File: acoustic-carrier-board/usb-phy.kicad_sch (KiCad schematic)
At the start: 53 parts, among them J801 TYPE-C-31-M-12, U801 USB3300-EZK, U802 LMV321, Y801 Crystal_GND24_Small

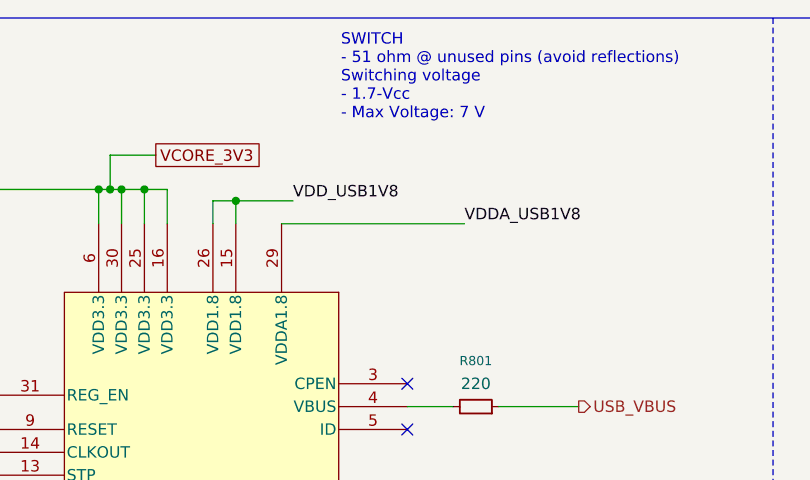
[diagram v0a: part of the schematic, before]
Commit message: Modified readme, removed testpoints and stubs, changed simulation folder structure, removed excess length matching
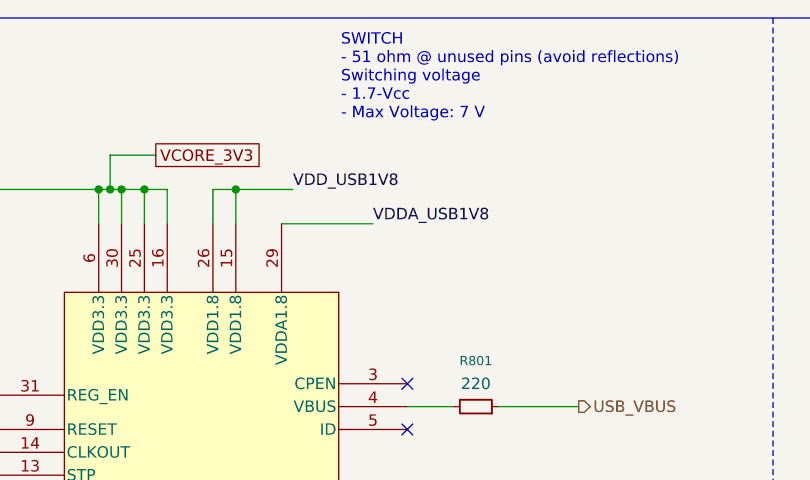
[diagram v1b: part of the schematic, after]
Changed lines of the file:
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@@
+	)
+	(junction
+		(at 160.02 38.1)
+		(diameter 0)
+		(color 0 0 0 0)
 	)
 	(junction
@@
 	(junction
 		(at 185.42 105.41)
-		(diameter 0)
-		(color 0 0 0 0)
-	)
-	(junction
-		(at 160.02 39.37)
 		(diameter 0)
 		(color 0 0 0 0)
@@
 	(wire
 		(pts
-			(xy 157.48 39.37) (xy 157.48 41.91)
+			(xy 157.48 38.1) (xy 157.48 41.91)
 		)
 		(stroke
@@
 	(wire
 		(pts
-			(xy 165.1 41.91) (xy 185.42 41.91)
+			(xy 165.1 41.91) (xy 175.26 41.91)
 		)
 		(stroke
@@
 	(wire
 		(pts
-			(xy 160.02 39.37) (xy 160.02 41.91)
+			(xy 160.02 38.1) (xy 160.02 41.91)
 		)
 		(stroke
@@
 	(wire
 		(pts
-			(xy 160.02 39.37) (xy 166.37 39.37)
+			(xy 160.02 38.1) (xy 166.37 38.1)
 		)
 		(stroke
@@
 	(wire
 		(pts
-			(xy 160.02 39.37) (xy 157.48 39.37)
+			(xy 160.02 38.1) (xy 157.48 38.1)
 		)
 		(stroke
@@
 	)
 	(label "VDD_USB1V8"
-		(at 166.37 39.37 0)
+		(at 166.37 38.1 0)
 		(effects
 			(font
@@
 	)
 	(label "VDDA_USB1V8"
-		(at 185.42 41.91 0)
+		(at 175.26 41.91 0)
 		(effects
 			(font

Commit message: added step-files
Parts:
- C801, C807, C808, C809, C810, C811, C812, C816, C820, C821, C822: LCSC Part Number (none) -> C22435929; LPN C22435929 -> (none); MPN CGA0201X7R104K160ET -> (none); Manufacturing Part Number (none) -> CGA0201X7R104K160ET
- C802, C817, C825: LCSC Part Number (none) -> C285010; LPN C285010 -> (none); MPN 0201B103K250NT -> (none); Manufacturing Part Number (none) -> 0201B103K250NT
- C803, C806: LCSC Part Number (none) -> C1555; LPN C1555 -> (none); MPN 0402CG220J500NT -> (none); Manufacturing Part Number (none) -> 0402CG220J500NT
- C804, C805: LCSC Part Number (none) -> C1530; LPN C1530 -> (none); MPN 0402B221K500NT -> (none); Manufacturing Part Number (none) -> 0402B221K500NT
- C813, C814, C819: LCSC Part Number (none) -> C23733; LPN C23733 -> (none); MPN CL05A475MP5NRNC -> (none); Manufacturing Part Number (none) -> CL05A475MP5NRNC
- C815: LCSC Part Number (none) -> C9196; LPN C9196 -> (none); MPN 1206B102K202NT -> (none); Manufacturing Part Number (none) -> 1206B102K202NT
- D801, D802: LCSC Part Number (none) -> C2286; LPN C2286 -> (none); MPN KT-0603R -> (none); Manufacturing Part Number (none) -> KT-0603R
- J801: LCSC Part Number (none) -> C165948; LPN C165948 -> (none); MPN TYPE-C-31-M-12 -> (none); Manufacturing Part Number (none) -> TYPE-C-31-M-12
- L801: LCSC Part Number (none) -> C113030; LPN C113030 -> (none); MPN BLM18SG121TN1D -> (none); Manufacturing Part Number (none) -> BLM18SG121TN1D
- R801: LCSC Part Number (none) -> C22962; LPN C22962 -> (none); MPN 0603WAF2200T5E -> (none); Manufacturing Part Number (none) -> 0603WAF2200T5E
- R802, R812: LCSC Part Number (none) -> C23018; LPN C23018 -> (none); MPN 0603WAF3901T5E -> (none); Manufacturing Part Number (none) -> 0603WAF3901T5E
- R803, R811: LCSC Part Number (none) -> C25803; LPN C25803 -> (none); MPN 0603WAF1003T5E -> (none); Manufacturing Part Number (none) -> 0603WAF1003T5E
- R804, R805: LCSC Part Number (none) -> C23186; LPN C23186 -> (none); MPN 0603WAF5101T5E -> (none); Manufacturing Part Number (none) -> 0603WAF5101T5E
- R806: LCSC Part Number (none) -> C26083; LPN C26083 -> (none); MPN 0402WGF1004TCE -> (none); Manufacturing Part Number (none) -> 0402WGF1004TCE
- R807: LCSC Part Number (none) -> C17168; LPN C17168 -> (none); MPN 0402WGF0000TCE -> (none); Manufacturing Part Number (none) -> 0402WGF0000TCE
- R808: LCSC Part Number (none) -> C22790; LPN C22790 -> (none); MPN 0603WAF1202T5E -> (none); Manufacturing Part Number (none) -> 0603WAF1202T5E
- R809, R810: LCSC Part Number (none) -> C4216; LPN C4216 -> (none); MPN 0603WAF3302T5E -> (none); Manufacturing Part Number (none) -> 0603WAF3302T5E
- R813, R821: LCSC Part Number (none) -> C23182; LPN C23182 -> (none); MPN 0603WAF470JT5E -> (none); Manufacturing Part Number (none) -> 0603WAF470JT5E
- R814, R826: LCSC Part Number (none) -> C23162; LPN C23162 -> (none); MPN 0603WAF4701T5E -> (none); Manufacturing Part Number (none) -> 0603WAF4701T5E
- R815, R830: LCSC Part Number (none) -> C21190; LPN C21190 -> (none); MPN 0603WAF1001T5E -> (none); Manufacturing Part Number (none) -> 0603WAF1001T5E
- R816: LCSC Part Number (none) -> C23206; LPN C23206 -> (none); MPN 0603WAF5602T5E -> (none); Manufacturing Part Number (none) -> 0603WAF5602T5E
- R817: LCSC Part Number (none) -> C21189; LPN C21189 -> (none); MPN 0603WAF0000T5E -> (none); Manufacturing Part Number (none) -> 0603WAF0000T5E
- R818: LCSC Part Number (none) -> C23260; LPN C23260 -> (none); MPN 0603WAF9101T5E -> (none); Manufacturing Part Number (none) -> 0603WAF9101T5E
- TP801: now left out of the parts list
- U801: LCSC Part Number (none) -> C108383; LPN C108383 -> (none); MPN USB3300-EZK-TR -> (none); Manufacturing Part Number (none) -> USB3300-EZK-TR
- U802: LCSC Part Number (none) -> C7972; LPN C7972 -> (none); MPN LMV321IDBVR -> (none); Manufacturing Part Number (none) -> LMV321IDBVR
- U803, U804: LCSC Part Number (none) -> C3035955; LPN C3035955 -> (none); MPN COS3201TR -> (none); Manufacturing Part Number (none) -> COS3201TR
- Y801: LCSC Part Number (none) -> C15643; LPN C15643 -> (none); MPN X322524MSB4SI -> (none); Manufacturing Part Number (none) -> X322524MSB4SI

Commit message: order carrier board
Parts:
- L801: LCSC Part Number C113030 -> C285595; Manufacturing Part Number BLM18SG121TN1D -> UPB160805T-121Y-N
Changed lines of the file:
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@@
 			)
 		)
-		(property "LCSC Part Number" "C113030"
+		(property "LCSC Part Number" "C285595"
 			(at 313.69 49.53 90)
 			(effects
@@
 			)
 		)
-		(property "Manufacturing Part Number" "BLM18SG121TN1D"
+		(property "Manufacturing Part Number" "UPB160805T-121Y-N "
 			(at 313.69 49.53 90)
 			(effects
